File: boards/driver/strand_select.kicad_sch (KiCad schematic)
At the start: 16 parts, among them Q1 MMBT2222, Q2 MMBT2907, Q3 MMBT2222

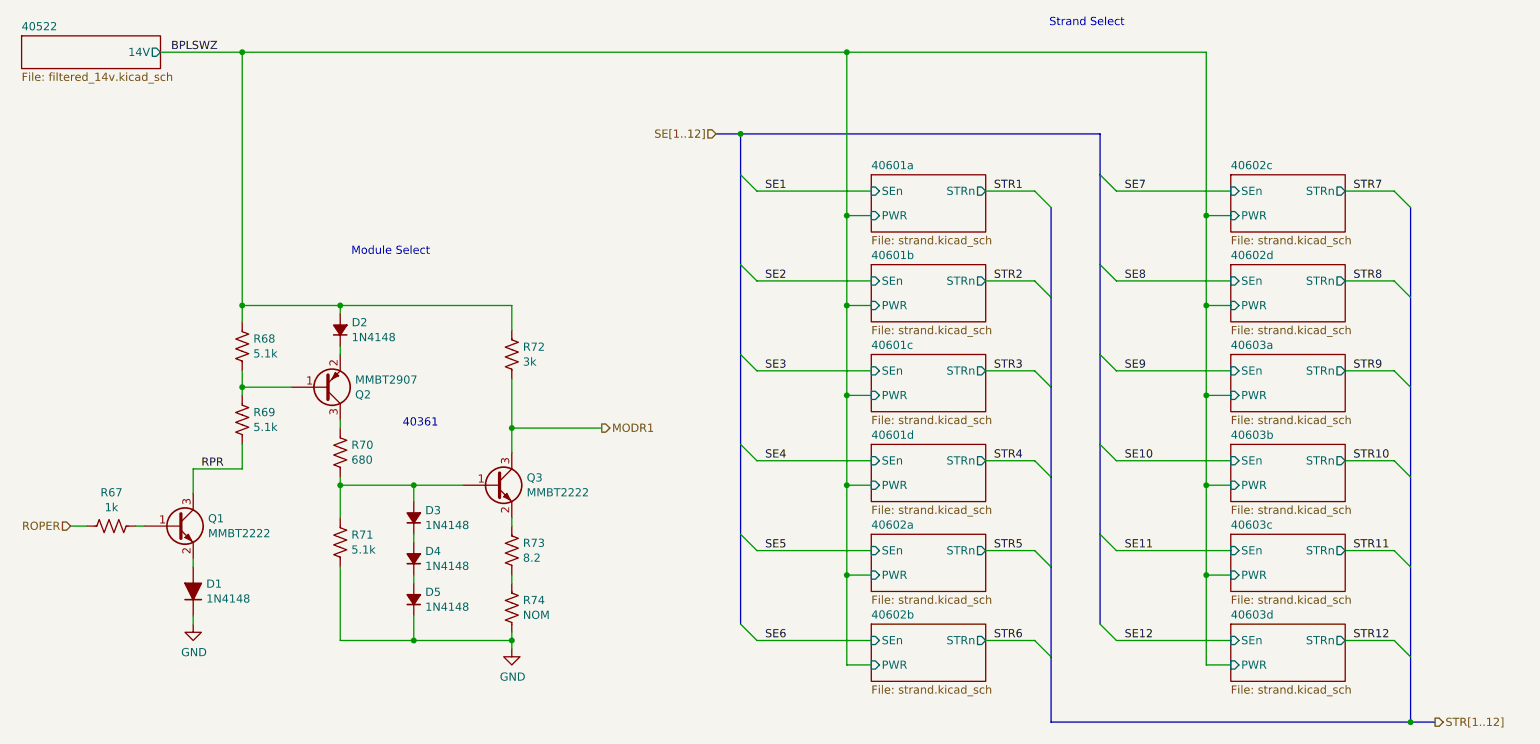
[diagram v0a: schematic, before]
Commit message: Driver: Added a 5V->3.3V LDO to replace the reversed cmod header, added jumpers for the 200R parallel returns, and renamed subcircuit ports to avoid unexpected ground connections.
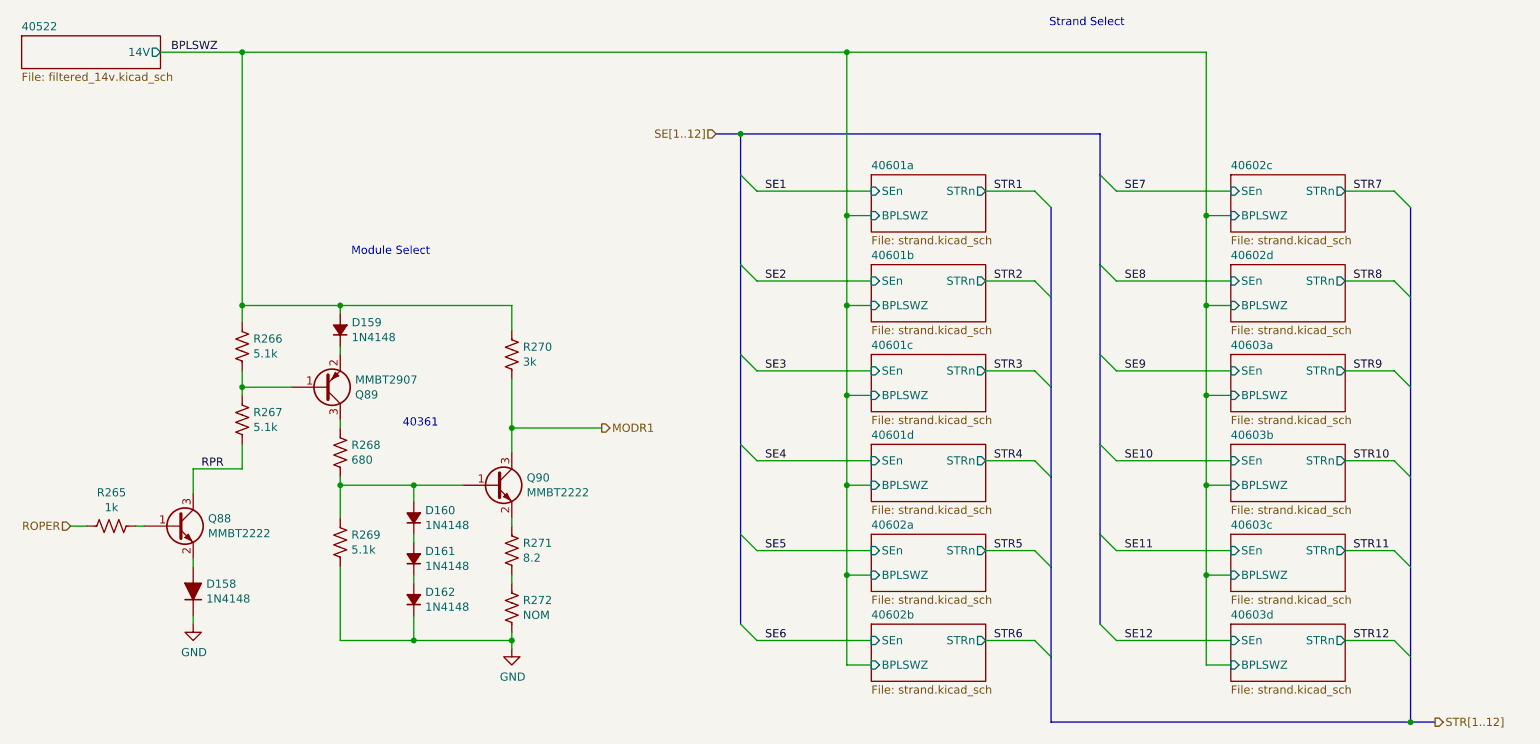
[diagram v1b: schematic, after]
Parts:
- renumbered D1 to D158, D2 to D159, D3 to D160, D4 to D161, D5 to D162, Q1 to Q88, Q2 to Q89, Q3 to Q90, R67 to R265, R68 to R266, R69 to R267, R70 to R268, R71 to R269, R72 to R270, R73 to R271, R74 to R272
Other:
- sheet 40601a ports: added BPLSWZ; removed PWR
- sheet 40601b ports: added BPLSWZ; removed PWR
- sheet 40601c ports: added BPLSWZ; removed PWR
- sheet 40601d ports: added BPLSWZ; removed PWR
- sheet 40602a ports: added BPLSWZ; removed PWR
- sheet 40602b ports: added BPLSWZ; removed PWR
- sheet 40602c ports: added BPLSWZ; removed PWR
- sheet 40602d ports: added BPLSWZ; removed PWR
- sheet 40603a ports: added BPLSWZ; removed PWR
- sheet 40603b ports: added BPLSWZ; removed PWR
- sheet 40603c ports: added BPLSWZ; removed PWR
- sheet 40603d ports: added BPLSWZ; removed PWR

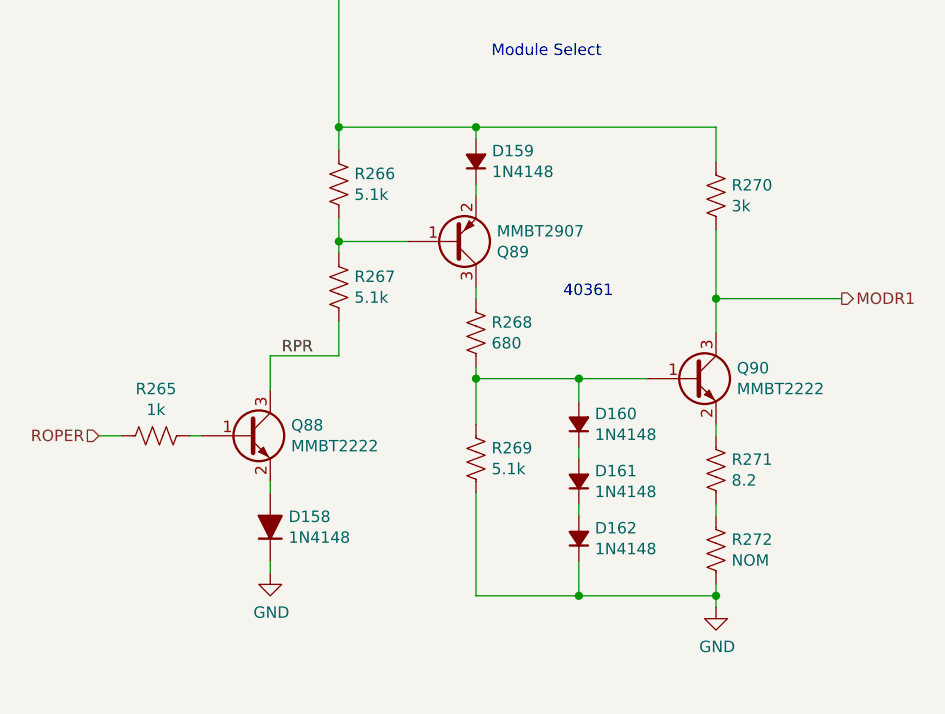
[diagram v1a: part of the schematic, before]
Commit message: Driver: incorporated most changes from the test board, and began layout
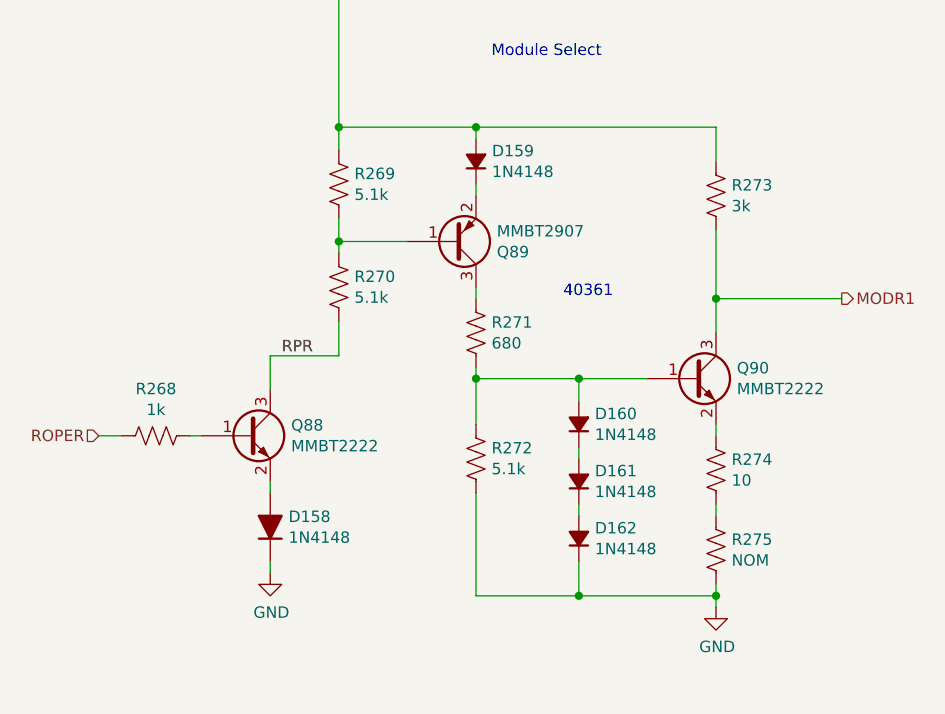
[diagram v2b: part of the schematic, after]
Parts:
- D158, D159, D160, D161, D162: footprint Diode_SMD:D_SOD-323 -> lachesis:D_SOD-323
- R274: renamed from R271; value 8.2 -> 10
- renumbered R265 to R268, R266 to R269, R267 to R270, R268 to R271, R269 to R272, R270 to R273, R272 to R275
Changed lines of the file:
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@@
   (symbol (lib_id "Device:R_US") (at 59.69 100.33 0) (unit 1)
     (in_bom yes) (on_board yes)
-    (property "Reference" "R267" (id 0) (at 61.4172 99.1616 0)
+    (property "Reference" "R270" (id 0) (at 61.4172 99.1616 0)
       (effects (font (size 1.27 1.27)) (justify left))
     )
@@
   (symbol (lib_id "Device:R_US") (at 59.69 88.9 0) (unit 1)
     (in_bom yes) (on_board yes)
-    (property "Reference" "R266" (id 0) (at 61.4172 87.7316 0)
+    (property "Reference" "R269" (id 0) (at 61.4172 87.7316 0)
       (effects (font (size 1.27 1.27)) (justify left))
     )
@@
   (symbol (lib_id "Device:R_US") (at 74.93 105.41 0) (unit 1)
     (in_bom yes) (on_board yes)
-    (property "Reference" "R268" (id 0) (at 76.6572 104.2416 0)
+    (property "Reference" "R271" (id 0) (at 76.6572 104.2416 0)
       (effects (font (size 1.27 1.27)) (justify left))
     )
@@
   (symbol (lib_id "Device:R_US") (at 74.93 119.38 0) (unit 1)
     (in_bom yes) (on_board yes)
-    (property "Reference" "R269" (id 0) (at 76.6572 118.2116 0)
+    (property "Reference" "R272" (id 0) (at 76.6572 118.2116 0)
       (effects (font (size 1.27 1.27)) (justify left))
     )
@@
       (effects (font (size 1.27 1.27)) (justify right))
     )
-    (property "Footprint" "Diode_SMD:D_SOD-323" (id 2) (at 74.93 86.36 90)
+    (property "Footprint" "lachesis:D_SOD-323" (id 2) (at 74.93 86.36 90)
       (effects (font (size 1.27 1.27)) hide)
     )
@@
       (effects (font (size 1.27 1.27)) (justify right))
     )
-    (property "Footprint" "Diode_SMD:D_SOD-323" (id 2) (at 86.36 115.57 90)
+    (property "Footprint" "lachesis:D_SOD-323" (id 2) (at 86.36 115.57 90)
       (effects (font (size 1.27 1.27)) hide)
     )
@@
       (effects (font (size 1.27 1.27)) (justify right))
     )
-    (property "Footprint" "Diode_SMD:D_SOD-323" (id 2) (at 86.36 121.92 90)
+    (property "Footprint" "lachesis:D_SOD-323" (id 2) (at 86.36 121.92 90)
       (effects (font (size 1.27 1.27)) hide)
     )
@@
       (effects (font (size 1.27 1.27)) (justify right))
     )
-    (property "Footprint" "Diode_SMD:D_SOD-323" (id 2) (at 86.36 128.27 90)
+    (property "Footprint" "lachesis:D_SOD-323" (id 2) (at 86.36 128.27 90)
       (effects (font (size 1.27 1.27)) hide)
     )
@@
   (symbol (lib_id "Device:R_US") (at 101.6 120.65 0) (unit 1)
     (in_bom yes) (on_board yes)
-    (property "Reference" "R271" (id 0) (at 103.3272 119.4816 0)
-      (effects (font (size 1.27 1.27)) (justify left))
-    )
-    (property "Value" "8.2" (id 1) (at 103.3272 121.793 0)
+    (property "Reference" "R274" (id 0) (at 103.3272 119.4816 0)
+      (effects (font (size 1.27 1.27)) (justify left))
+    )
+    (property "Value" "10" (id 1) (at 103.3272 121.793 0)
       (effects (font (size 1.27 1.27)) (justify left))
     )
@@
   (symbol (lib_id "Device:R_US") (at 101.6 129.54 0) (unit 1)
     (in_bom yes) (on_board yes)
-    (property "Reference" "R272" (id 0) (at 103.3272 128.3716 0)
+    (property "Reference" "R275" (id 0) (at 103.3272 128.3716 0)
       (effects (font (size 1.27 1.27)) (justify left))
     )
@@
   (symbol (lib_id "Device:R_US") (at 101.6 90.17 0) (unit 1)
     (in_bom yes) (on_board yes)
-    (property "Reference" "R270" (id 0) (at 103.3272 89.0016 0)
+    (property "Reference" "R273" (id 0) (at 103.3272 89.0016 0)
       (effects (font (size 1.27 1.27)) (justify left))
     )
@@
   (symbol (lib_id "Device:R_US") (at 39.37 116.84 270) (unit 1)
     (in_bom yes) (on_board yes)
-    (property "Reference" "R265" (id 0) (at 39.37 111.633 90))
+    (property "Reference" "R268" (id 0) (at 39.37 111.633 90))
     (property "Value" "1k" (id 1) (at 39.37 113.9444 90))
     (property "Footprint" "Resistor_SMD:R_0603_1608Metric" (id 2) (at 39.116 117.856 90)
@@
       (effects (font (size 1.27 1.27)) (justify right))
     )
-    (property "Footprint" "Diode_SMD:D_SOD-323" (id 2) (at 52.07 127 0)
+    (property "Footprint" "lachesis:D_SOD-323" (id 2) (at 52.07 127 0)
       (effects (font (size 1.27 1.27)) hide)
     )
@@
   (symbol (lib_id "power:GND") (at 52.07 132.08 0) (unit 1)
     (in_bom yes) (on_board yes)
-    (property "Reference" "#PWR0158" (id 0) (at 52.07 138.43 0)
+    (property "Reference" "#PWR0161" (id 0) (at 52.07 138.43 0)
       (effects (font (size 1.27 1.27)) hide)
     )
@@
   (symbol (lib_id "power:GND") (at 101.6 135.89 0) (unit 1)
     (in_bom yes) (on_board yes)
-    (property "Reference" "#PWR0159" (id 0) (at 101.6 142.24 0)
-      (effects (font (size 1.27 1.27)) hide)
-    )
+    (property "Reference" "#PWR0162" (id 0) (at 101.6 142.24 0)
+      (effects (font (size 1.27 1.27)) hide)
+    )

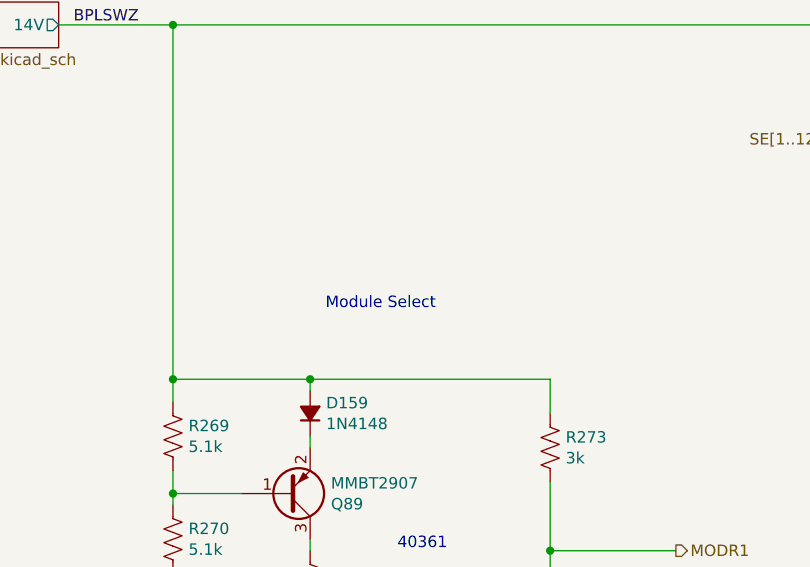
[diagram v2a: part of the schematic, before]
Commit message: Driver: 3.3V section is now laid out, contained entirely beneath the FPGA daughter board
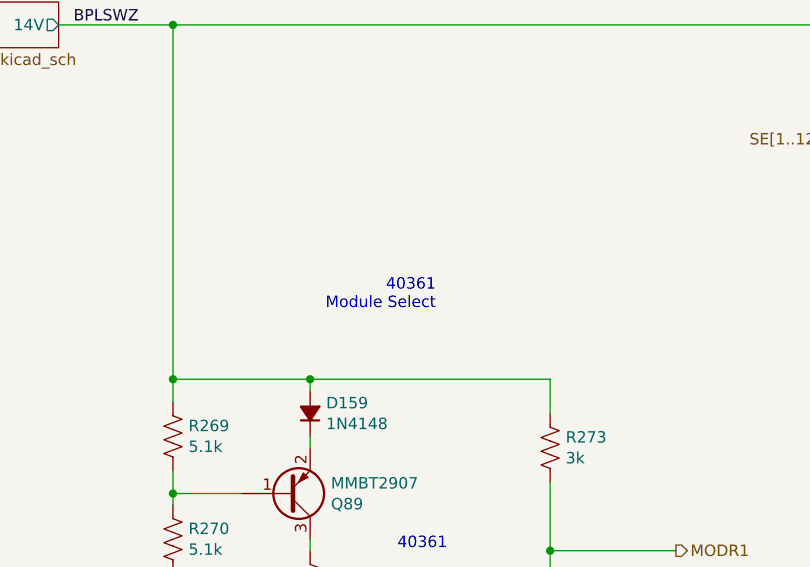
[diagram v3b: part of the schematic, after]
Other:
- note added: "40361 Module Select"
- note removed: "Module Select"
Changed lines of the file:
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@@
     (stroke (width 0) (type default) (color 0 0 0 0))
   )
-  (text "Module Select" (at 88.9 74.93 180)
+  (text "40361\nModule Select" (at 88.9 74.93 180)
     (effects (font (size 1.27 1.27)) (justify right bottom))
   )

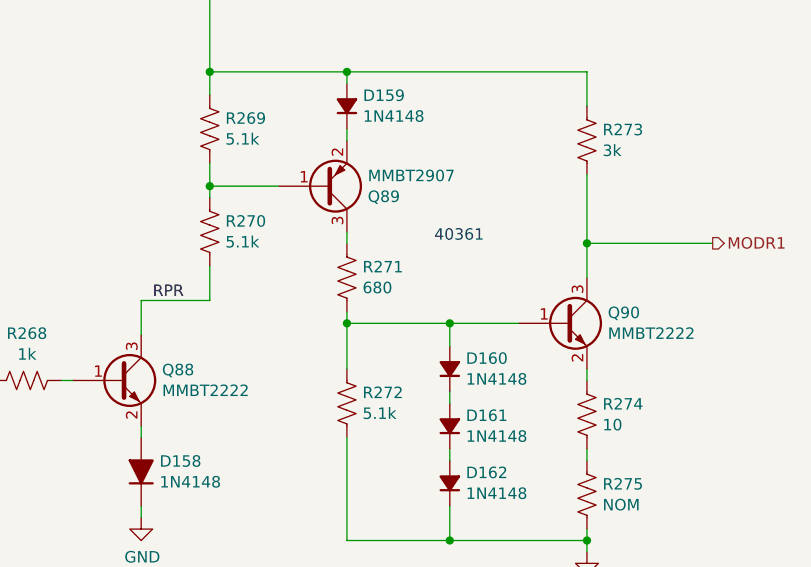
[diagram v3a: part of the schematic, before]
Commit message: Driver: incorporated completed backplane pinout and did a little bit more routing on the board
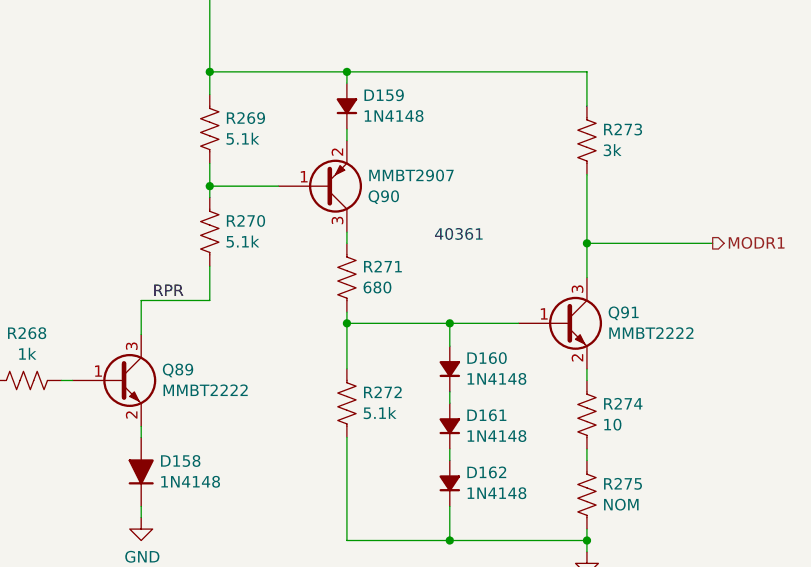
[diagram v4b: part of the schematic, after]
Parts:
- renumbered Q88 to Q89, Q89 to Q90, Q90 to Q91
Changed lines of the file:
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@@
   (symbol (lib_id "Device:Q_PNP_BEC") (at 72.39 95.25 0) (mirror x) (unit 1)
     (in_bom yes) (on_board yes)
-    (property "Reference" "Q89" (id 0) (at 77.2414 96.4184 0)
+    (property "Reference" "Q90" (id 0) (at 77.2414 96.4184 0)
       (effects (font (size 1.27 1.27)) (justify left))
     )
@@
   (symbol (lib_id "Device:Q_NPN_BEC") (at 99.06 110.49 0) (unit 1)
     (in_bom yes) (on_board yes)
-    (property "Reference" "Q90" (id 0) (at 103.9114 109.3216 0)
+    (property "Reference" "Q91" (id 0) (at 103.9114 109.3216 0)
       (effects (font (size 1.27 1.27)) (justify left))
     )
@@
   (symbol (lib_id "Device:Q_NPN_BEC") (at 49.53 116.84 0) (unit 1)
     (in_bom yes) (on_board yes)
-    (property "Reference" "Q88" (id 0) (at 54.3814 115.6716 0)
+    (property "Reference" "Q89" (id 0) (at 54.3814 115.6716 0)
       (effects (font (size 1.27 1.27)) (justify left))
     )
@@
   (symbol (lib_id "power:GND") (at 52.07 132.08 0) (unit 1)
     (in_bom yes) (on_board yes)
-    (property "Reference" "#PWR0161" (id 0) (at 52.07 138.43 0)
+    (property "Reference" "#PWR0160" (id 0) (at 52.07 138.43 0)
       (effects (font (size 1.27 1.27)) hide)
     )
@@
   (symbol (lib_id "power:GND") (at 101.6 135.89 0) (unit 1)
     (in_bom yes) (on_board yes)
-    (property "Reference" "#PWR0162" (id 0) (at 101.6 142.24 0)
-      (effects (font (size 1.27 1.27)) hide)
-    )
+    (property "Reference" "#PWR0161" (id 0) (at 101.6 142.24 0)
+      (effects (font (size 1.27 1.27)) hide)
+    )
